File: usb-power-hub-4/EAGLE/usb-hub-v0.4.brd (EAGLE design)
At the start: 95 x 25 mm, 37 parts, among them U1 RICHTEKRT9715AGBR, U2 RICHTEKRT9715AGBR, U3 RICHTEKRT9715AGBR, U4 RICHTEKRT9715AGBR

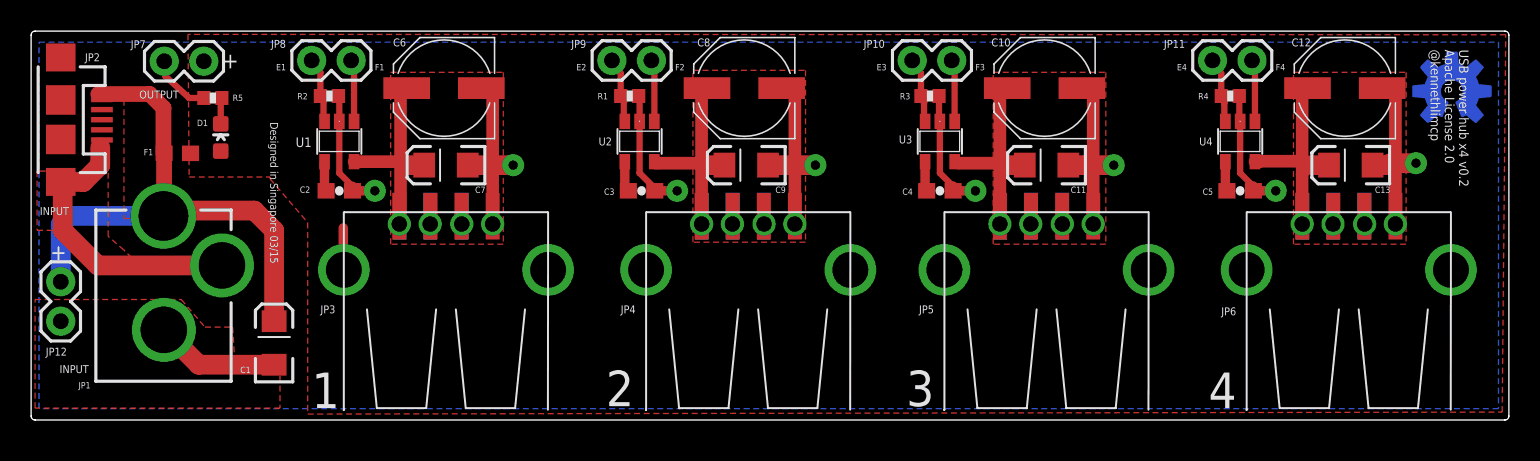
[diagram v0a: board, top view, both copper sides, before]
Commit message: V0.4 update!
- Improved DFM for R1 to R4

- Improved silkscreen text size and readibility
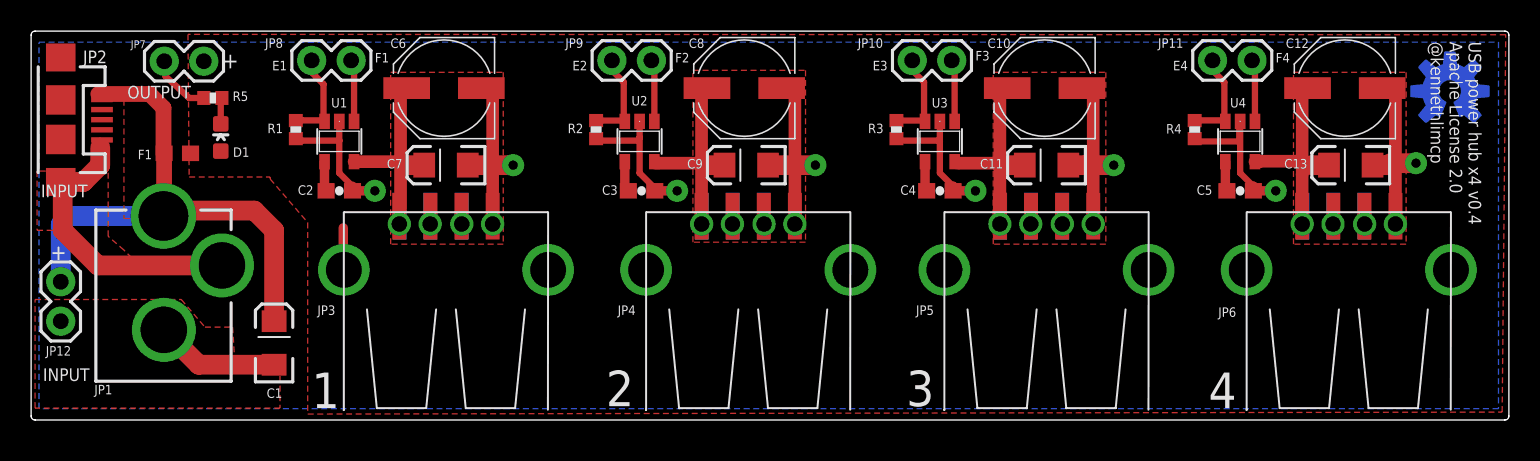
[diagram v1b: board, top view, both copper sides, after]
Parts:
- moved R1 21.6 mm to (17.0, 18.7), turned to 90 degrees
- moved R2 17.3 mm to (36.3, 18.7), turned to 90 degrees
- moved R4 3.14 mm to (74.8, 18.7), turned to 90 degrees
- moved R3 3.05 mm to (55.6, 18.7), turned to 90 degrees
- moved LOGO1 0.13 mm to (91.2, 21.1)
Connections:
- net EN1: now also R1.2; no longer R2.2
- net EN2: now also R2.2; no longer R1.2
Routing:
- net GND: track 99.7 -> 106.0 mm
- net EN4: track 4.16 -> 6.17 mm
- net EN3: track 4.16 -> 6.13 mm
- net EN2: track 4.26 -> 6.13 mm
- net EN1: track 4.33 -> 6.04 mm
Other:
- board text added: "USB power hub x4 v0.4 Apache License 2.0 @kennethlimcp"
- board text removed: "USB power hub x4 v0.2 Apache License 2.0 @kennethlimcp"
